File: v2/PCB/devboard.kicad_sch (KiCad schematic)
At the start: 33 parts, among them J1 USB_C_Receptacle_USB2.0_14P, J2 Conn_01x20, J3 Conn_01x20, J4 Conn_01x03, SW1 SW_Push, U1 RP2040, U2 MCP1700x-330xxTT, U3 W25Q16JVUXIQ TR, U4 BMI160, Y1 Crystal_GND24

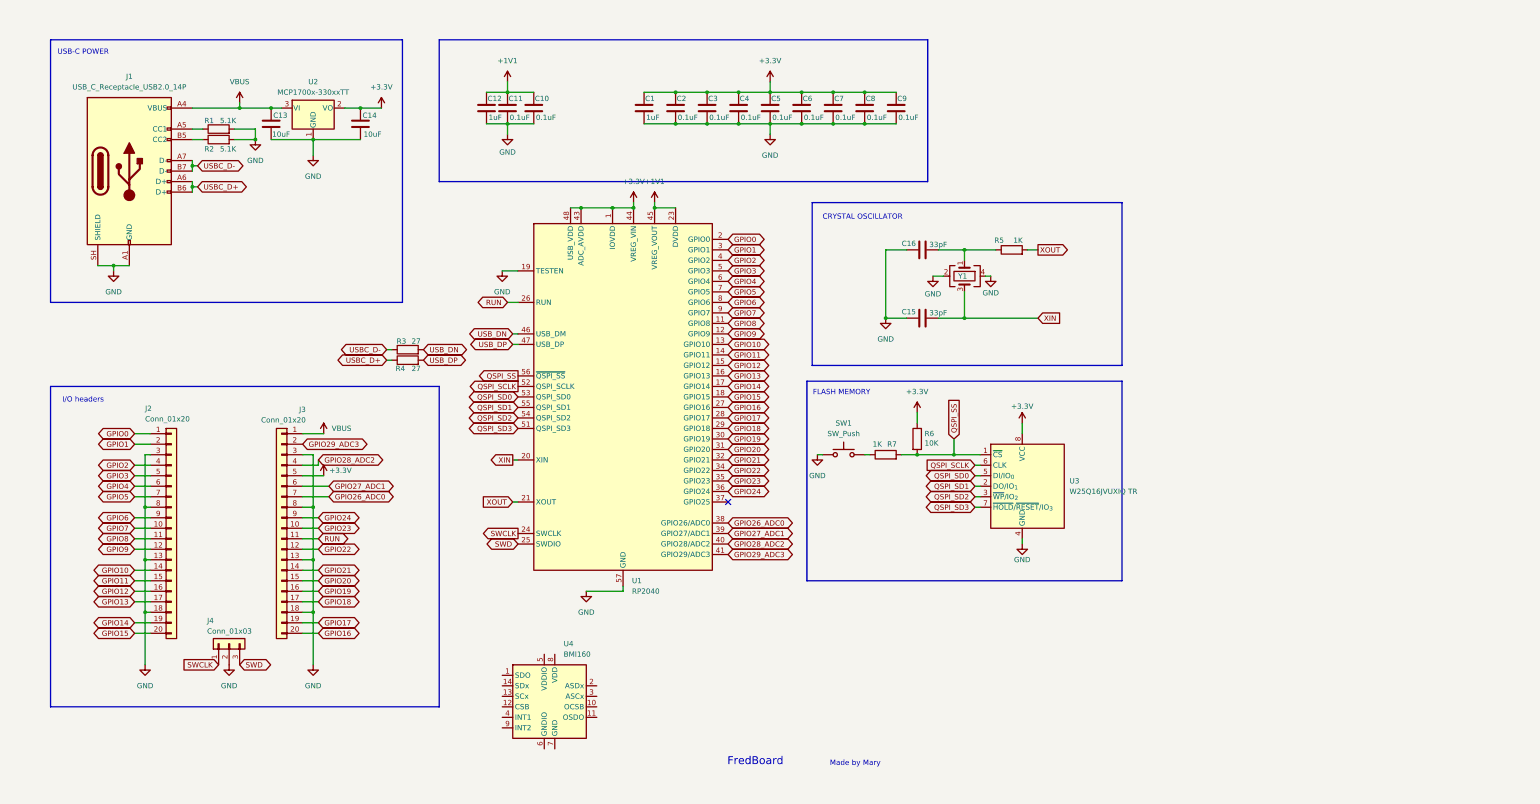
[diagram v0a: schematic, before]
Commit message: added imu to the v2 and created/wired pcb
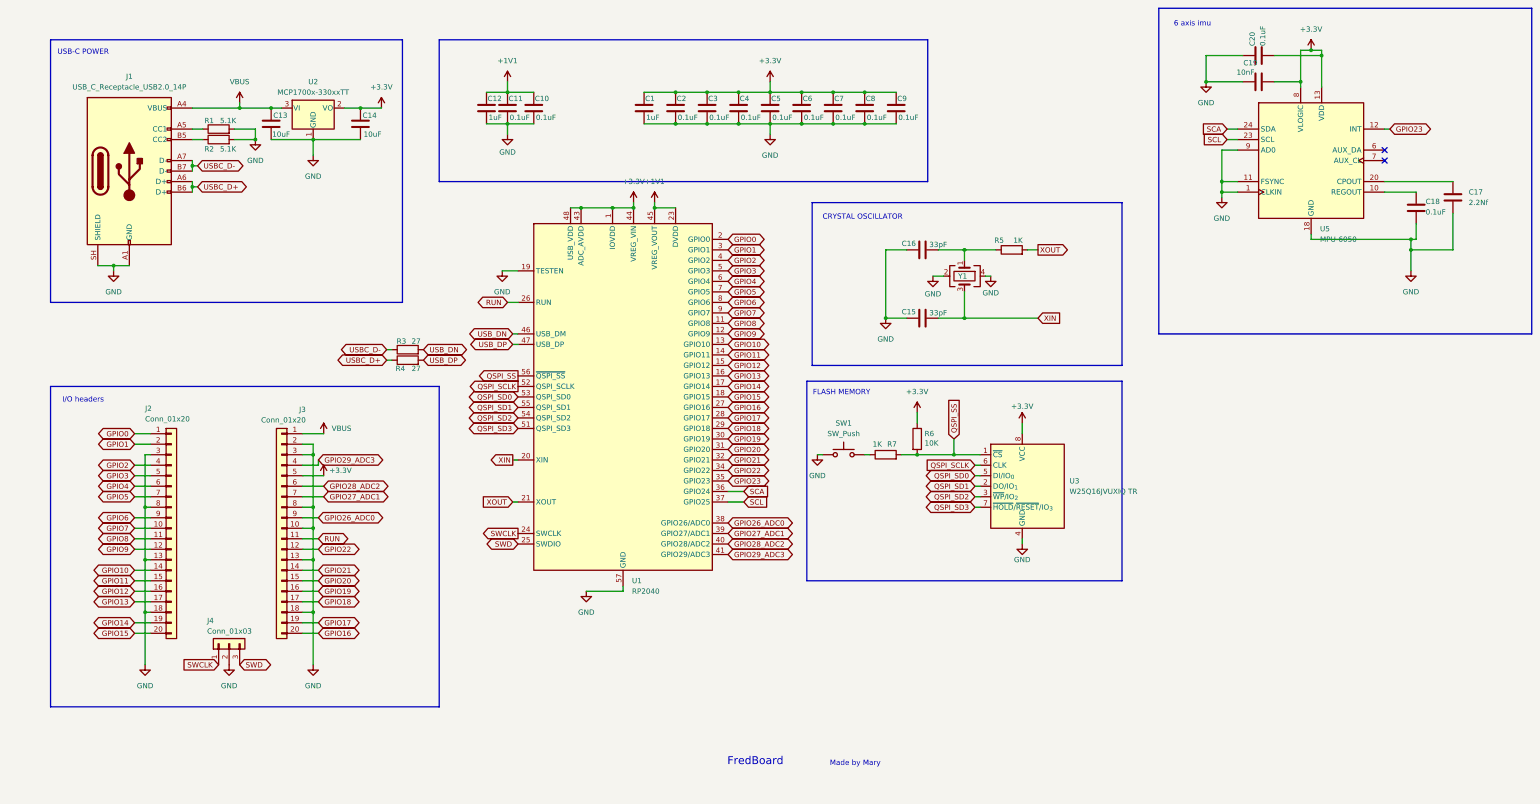
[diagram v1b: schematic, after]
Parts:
- removed U4: BMI160, Package_LGA:Bosch_LGA-14_3x2.5mm_P0.5mm, symbol Sensor_Motion:BMI160
- added C17: 2.2Nf, Capacitor_SMD:C_0402_1005Metric, symbol Device:C
- added C18, C20: 0.1uF, Capacitor_SMD:C_0402_1005Metric, symbol Device:C
- added C19: 10nF, Capacitor_SMD:C_0402_1005Metric, symbol Device:C
- added U5: MPU-6050, Sensor_Motion:InvenSense_QFN-24_4x4mm_P0.5mm, symbol Sensor_Motion:MPU-6050
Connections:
- net +3.3V: now also C19.2, C20.2, U5.13 (VDD), U5.8 (VLOGIC)
- net GND: now also J3.10 (Pin_10), J3.2 (Pin_2), C17.2, C18.2, C19.1, C20.1, U5.1 (CLKIN), U5.11 (FSYNC), U5.18 (GND), U5.9 (AD0)
- net GPIO23: now also U5.12 (INT); no longer J3.10 (Pin_10)
- net GPIO26_ADC0: now also J3.9 (Pin_9); no longer J3.7 (Pin_7)
- net GPIO27_ADC1: now also J3.7 (Pin_7); no longer J3.6 (Pin_6)
- net GPIO28_ADC2: now also J3.6 (Pin_6); no longer J3.4 (Pin_4)
- net GPIO29_ADC3: now also J3.4 (Pin_4); no longer J3.2 (Pin_2)
- net SCL: now reaches U1.37 (GPIO25)
- net SCL: now also U5.23 (SCL)
- net GPIO24 renamed SCA
- net SCA: now also U5.24 (SDA); no longer J3.9 (Pin_9)
- new net: C17.1, U5.20 (CPOUT)
- new net: C18.1, U5.10 (REGOUT)
- no-connect marks 1 -> 2
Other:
- note added: "6 axis imu"

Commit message: updated pcb and made renders
-Changed imu to a MPU-6500
-moved some traces and changed some pads in the devboard
-remade gerber and BOM
-created renders of the v2
-made pinout image of the v2
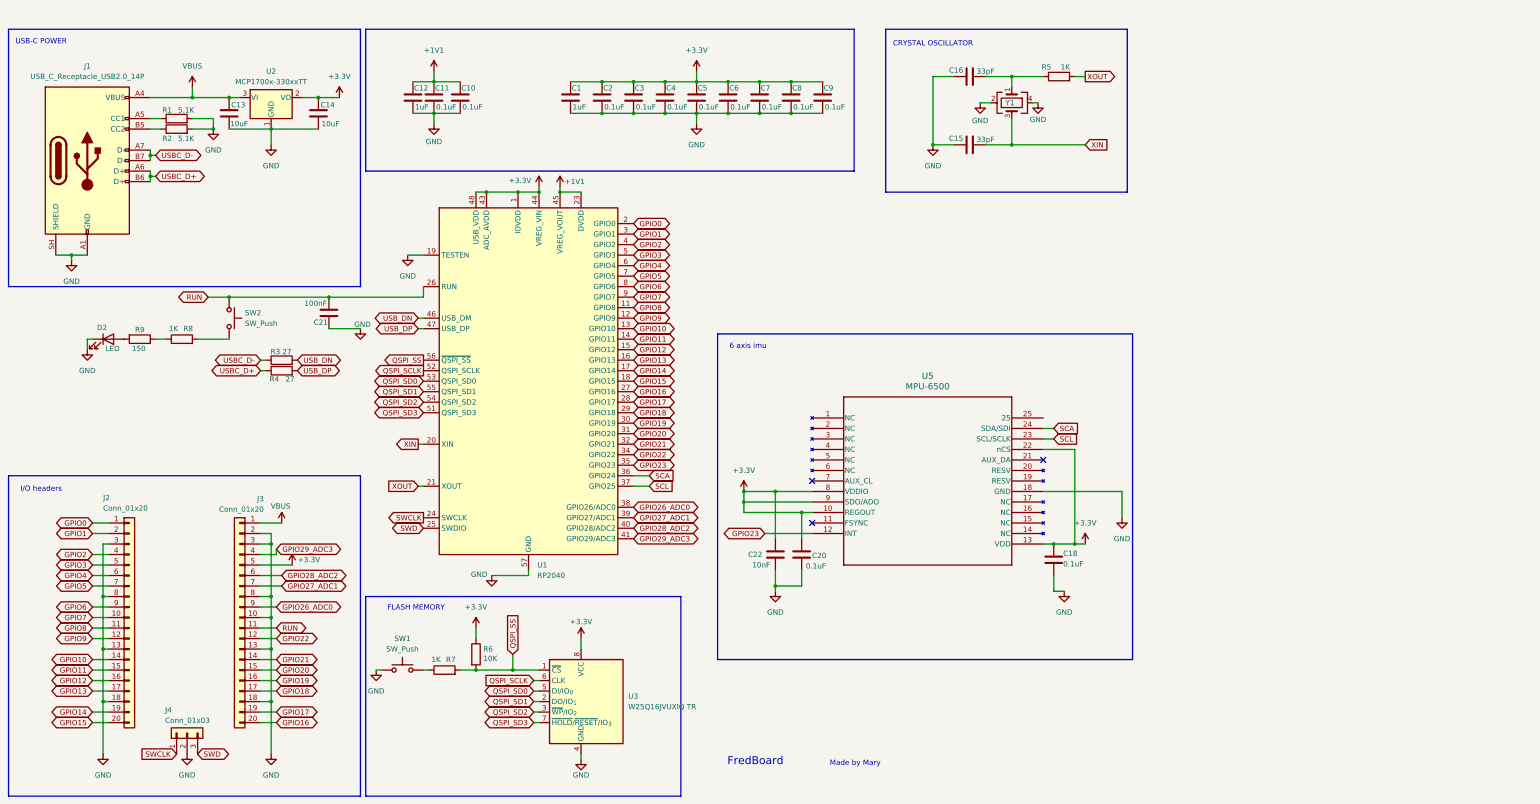
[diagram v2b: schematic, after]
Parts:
- removed C17: 2.2Nf, Capacitor_SMD:C_0402_1005Metric, symbol Device:C
- removed C19: 10nF, Capacitor_SMD:C_0402_1005Metric, symbol Device:C
- removed U5: MPU-6050, Sensor_Motion:InvenSense_QFN-24_4x4mm_P0.5mm, symbol Sensor_Motion:MPU-6050
- added C21: 100nF, Capacitor_SMD:C_0402_1005Metric, symbol Device:C
- added C22: 10nF, Capacitor_SMD:C_0402_1005Metric, symbol Device:C
- added D2: LED, LED_SMD:LED_0402_1005Metric, symbol Device:LED
- added R8: 1K, Resistor_SMD:R_0402_1005Metric, symbol Device:R
- added R9: 150, Resistor_SMD:R_0402_1005Metric, symbol Device:R
- added SW2: SW_Push, Button_Switch_SMD:SW_Push_SPST_NO_Alps_SKRK, symbol Switch:SW_Push
- added U5: MPU-6500, mpu 6500:QFN24_3X3X0P9_IVS, symbol 2026-07-21_11-32-29:MPU-6500
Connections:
- net +3.3V: now also C18.1, C20.1, C22.1, U5.10 (REGOUT), U5.13 (VDD), U5.22 (nCS), U5.8 (VDDIO), U5.9 (SDO/ADO); no longer C20.2
- net GND: now also C20.2, C21.1, C22.2, D2.1 (K), U5.18 (GND); no longer C20.1
- net GPIO23: now also U5.12 (INT)
- net RUN: now also C21.2, SW2.1
- net SCA: now also U5.24 (SDA/SDI)
- net SCL: now also U5.23 (SCL/SCLK)
- new net: R8.1, R9.1
- new net: R8.2, SW2.2
- new net: D2.2 (A), R9.2
- no-connect marks 2 -> 3
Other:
- moved on the sheet: C1, C10, C11, C12, C13, C14, C15, C16, C18, C2, C20, C3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
